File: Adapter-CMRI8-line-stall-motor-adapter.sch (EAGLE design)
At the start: 15 parts, among them M1 MOUNTINGHOLE, M2 MOUNTINGHOLE

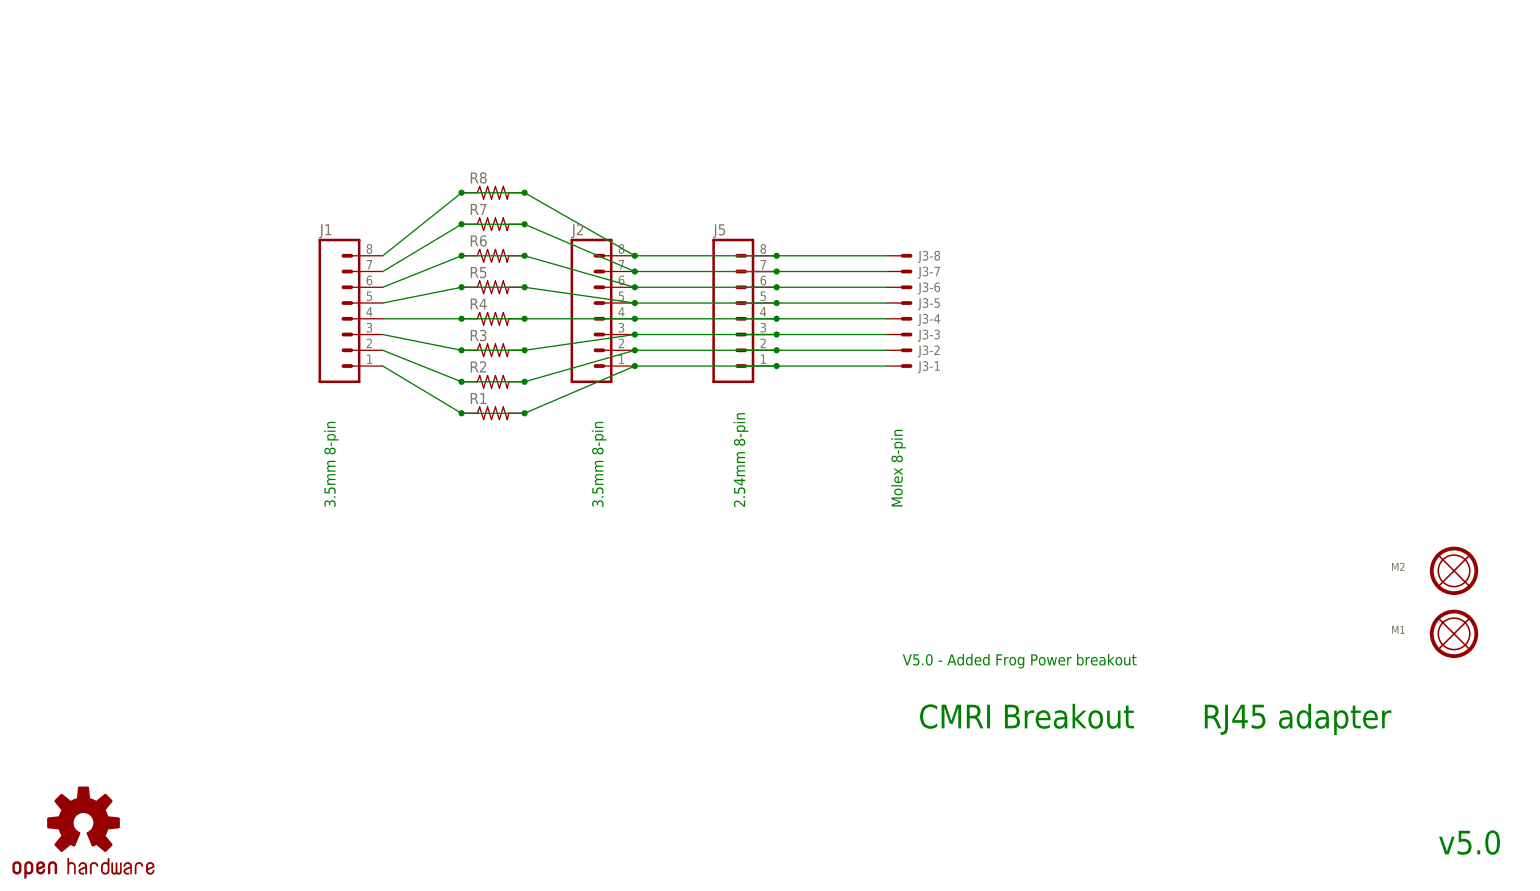
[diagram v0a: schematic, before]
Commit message: clean up of initial fab order
Misc changes to clean up clearances and documentation for initial build (20211204)
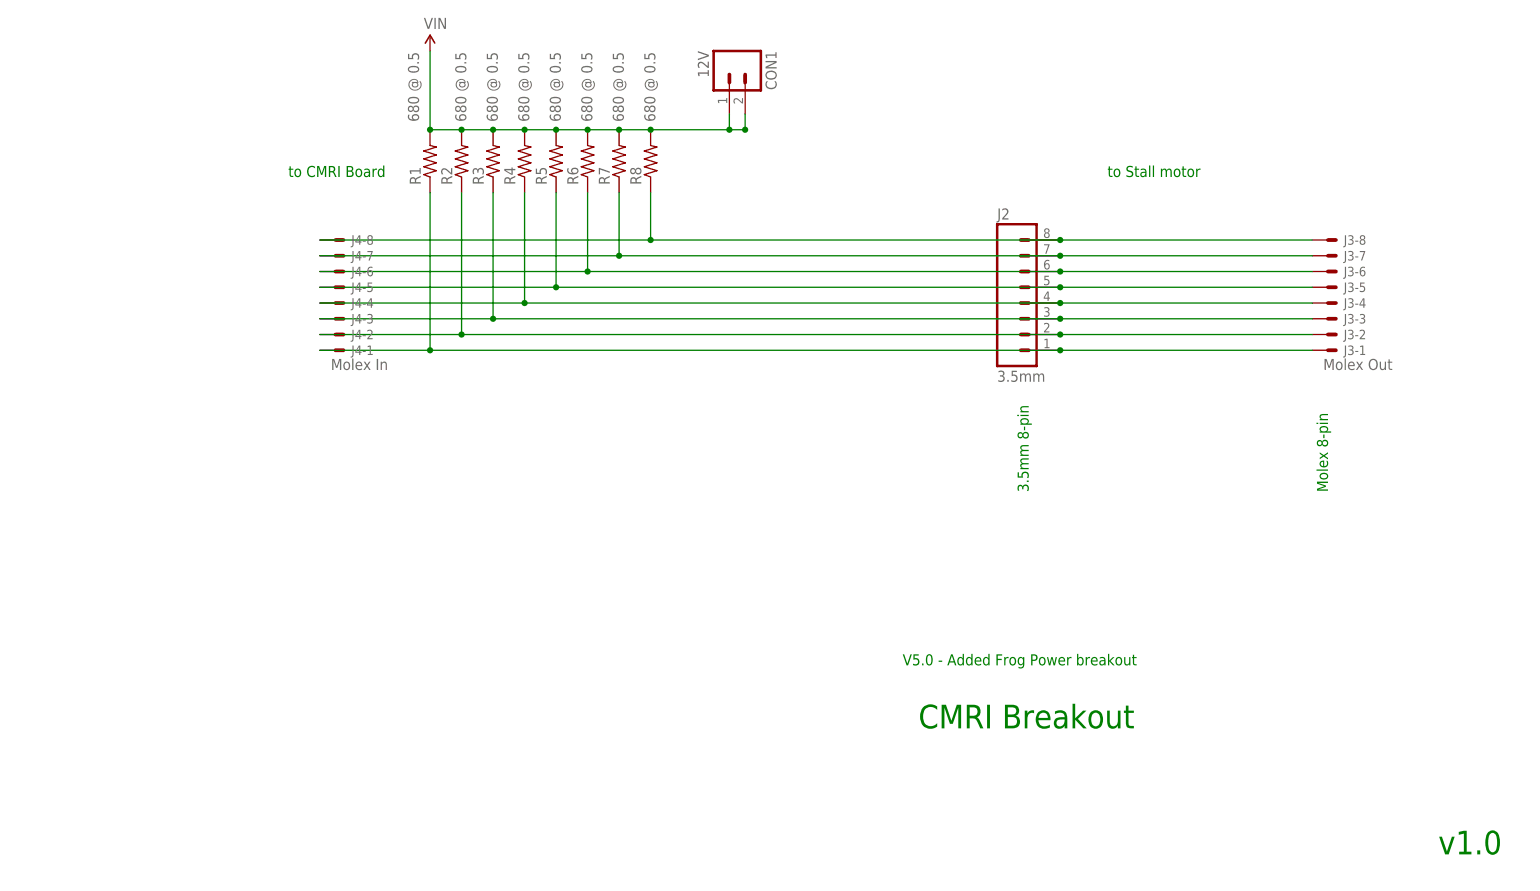
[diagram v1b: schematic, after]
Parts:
- removed J1: (no value), SPCoast:CONNECTOR-M083.5MM-8
- removed J5: (no value), SPCoast:CONNECTOR-M08LOCK
- removed M1, M2: MOUNTINGHOLE, SPCoast:MOUNTINGHOLE
- removed U$1: DOC-OSHW-LOGO-L, SPCoast:DOC-OSHW-LOGO-L
- added CON1: 12V, SPCoast:CONNECTOR-M023.5MM-LOCK
- added J4: Molex In, SPCoast:KK-156-8F
- J2: value (none) -> 3.5mm
- J3: value (none) -> Molex Out
- R1, R2, R3, R4, R5, R6, R7, R8: value (none) -> 680 @ 0.5; device SPCoast:RPTH04 -> SparkFun-Resistors:RESISTORPTH-1/2W
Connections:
- removed net L1: J1.1, J2.1, J3-1.S, J5.1, R1.1, R1.2
- removed net L4: J1.4, J2.4, J3-4.S, J5.4, R4.1, R4.2
- new net N$1: J2.1, J3-1.S, J4-1.S, R1.1
- new net N$8: J2.4, J3-4.S, J4-4.S, R4.1
- new net VIN: CON1.A, CON1.B, R1.2, R2.2, R3.2, R4.2, R5.2, R6.2, R7.2, R8.2
- net L2: now also J4-2.S; no longer J1.2, J5.2, R2.2
- net L3: now also J4-3.S; no longer J1.3, J5.3, R3.2
- net L5: now also J4-5.S; no longer J1.5, J5.5, R5.2
- net L6: now also J4-6.S; no longer J1.6, J5.6, R6.2
- net L7: now also J4-7.S; no longer J1.7, J5.7, R7.2
- net L8: now also J4-8.S; no longer J1.8, J5.8, R8.2
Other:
- note added: "to CMRI Board"
- note added: "to Stall motor"
- note added: "v1.0"
- note removed: "2.54mm 8-pin"
- note removed: "RJ45 adapter"
- note removed: "v5.0"
- moved on the sheet: J2, J3-1, J3-2, J3-3, J3-4, J3-5, J3-6, J3-7, J3-8
